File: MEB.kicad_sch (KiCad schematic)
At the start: 6 parts, among them J7 171857-0003, J8 171856-0004

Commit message: Cleanup symbol field table
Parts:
- D2: ALTIUM_VALUE 3.2V -> (none); DATASHEET LINK https://www.we-online.com/katalog/datasheet/150080BS75000.p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 -> (none); MANUFACTURER Würth Elektronik -> (none); MANUFACTURER PART NUMBER 150080BS75000 -> (none); OPERATING TEMPERATURE -40°C ~ 85°C -> (none); PACKAGE / CASE 0805 (2012 Metric) -> (none); Part Number (none) -> 150080BS75000; ROHS YES -> (none)
- D3: ALTIUM_VALUE 3.2V -> (none); DATASHEET LINK https://www.we-online.com/katalog/datasheet/150080GS75000.p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 -> (none); MANUFACTURER Würth Elektronik -> (none); MANUFACTURER PART NUMBER 150080GS75000 -> (none); OPERATING TEMPERATURE -40°C ~ 85°C -> (none); PACKAGE / CASE 0805 (2012 Metric) -> (none); Part Number (none) -> 150080GS75000; ROHS YES -> (none)
- J7: ALTIUM_VALUE 1x3 -> (none); DATASHEET LINK https://componentsearchengine.com//171857-0003.pdf -> (none); MANUFACTURER Molex -> (none); MANUFACTURER PART NUMBER 171857-0003 -> (none); MANUFACTURER_NAME Molex -> (none); MOUSER2 PART NUMBER 538-171857-0003 -> (none); MOUSER2 PRICE/STOCK https://www.mouser.com/Search/Refine.aspx?Keyword=538-17185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 -> (none); Part Number (none) -> 171857-0003
- J8: ALTIUM_VALUE 1x4 -> (none); DATASHEET LINK https://www.molex.com/pdm_docs/sd/1718560004_sd.pdf -> (none); HEIGHT 11.05mm -> (none); MANUFACTURER Molex -> (none); MANUFACTURER PART NUMBER 171856-0004 -> (none); MANUFACTURER_NAME Molex -> (none); Part Number (none) -> 171856-0004
- R11: ALTIUM_VALUE 1.3k -> (none); DATASHEET LINK https://www.koaspeer.com/pdfs/RK73B.pdf -> (none); MANUFACTURER KOA Speer Electronics, Inc. -> (none); MANUFACTURER PART NUMBER RK73B2ATTD132J -> (none); OPERATING TEMPERATURE -55°C ~ 155°C -> (none); PACKAGE / CASE 0805 (2012 Metric) -> (none); Part Number (none) -> RK73B2ATTD132J; ROHS YES -> (none)
- R12: ALTIUM_VALUE 10 -> (none); DATASHEET LINK https://www.yageo.com/upload/media/product/productsearch/da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 -> (none); MANUFACTURER YAGEO -> (none); MANUFACTURER PART NUMBER RC0805FR-0710RL -> (none); OPERATING TEMPERATURE -55°C ~ 155°C -> (none); PACKAGE / CASE 0805 (2012 Metric) -> (none); Part Number (none) -> RC0805FR-0710RL; ROHS YES -> (none)

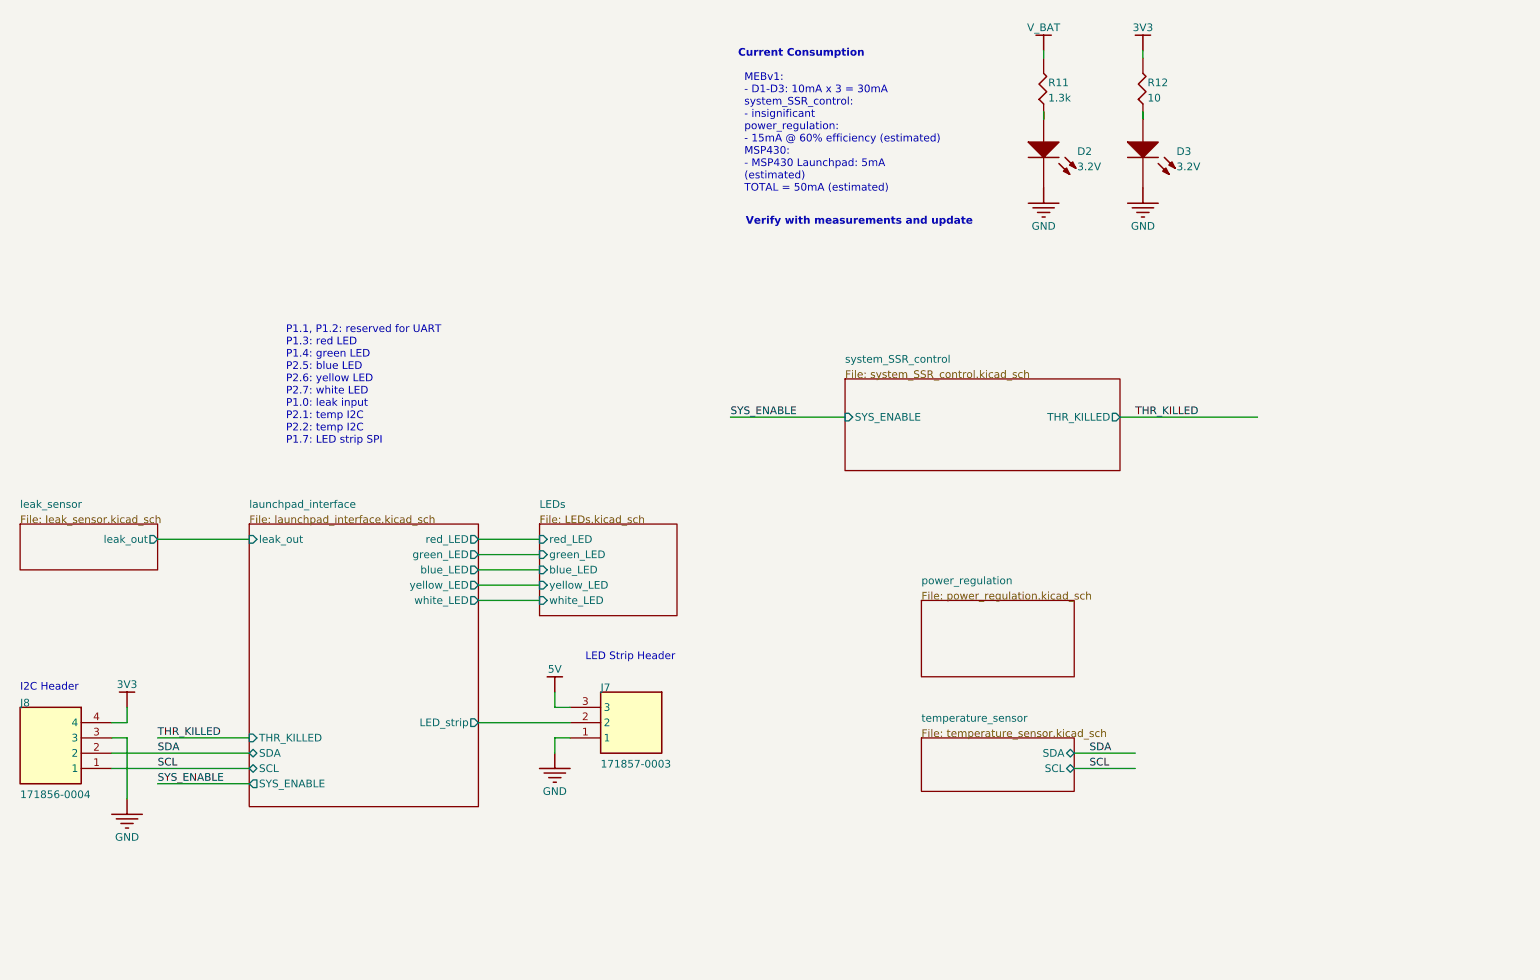
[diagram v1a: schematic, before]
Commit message: Input and Output Header Updates to MEB
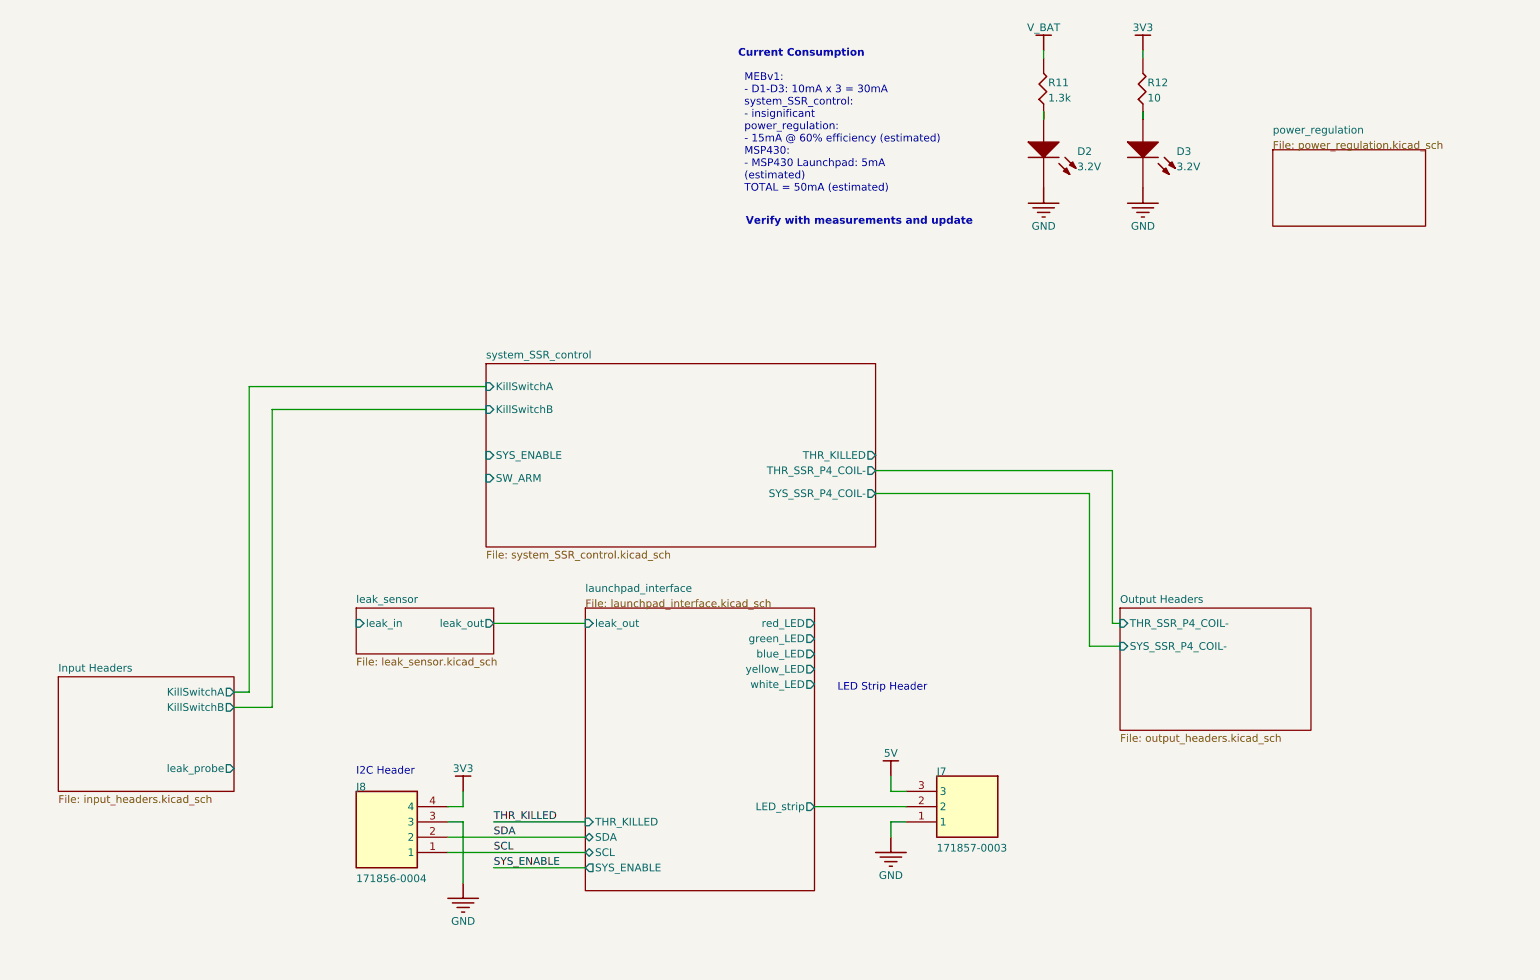
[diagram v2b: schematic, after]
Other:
- removed sheet LEDs
- removed sheet temperature_sensor
- added sheet Input Headers (input_headers.kicad_sch)
- added sheet Output Headers (output_headers.kicad_sch)
- sheet leak_sensor ports: added leak_in; removed none
- sheet system_SSR_control ports: added KillSwitchA, KillSwitchB, SW_ARM, SYS_SSR_P4_COIL-, THR_SSR_P4_COIL-; removed none
- moved on the sheet: J7, J8

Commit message: Finished updating all input and output headers
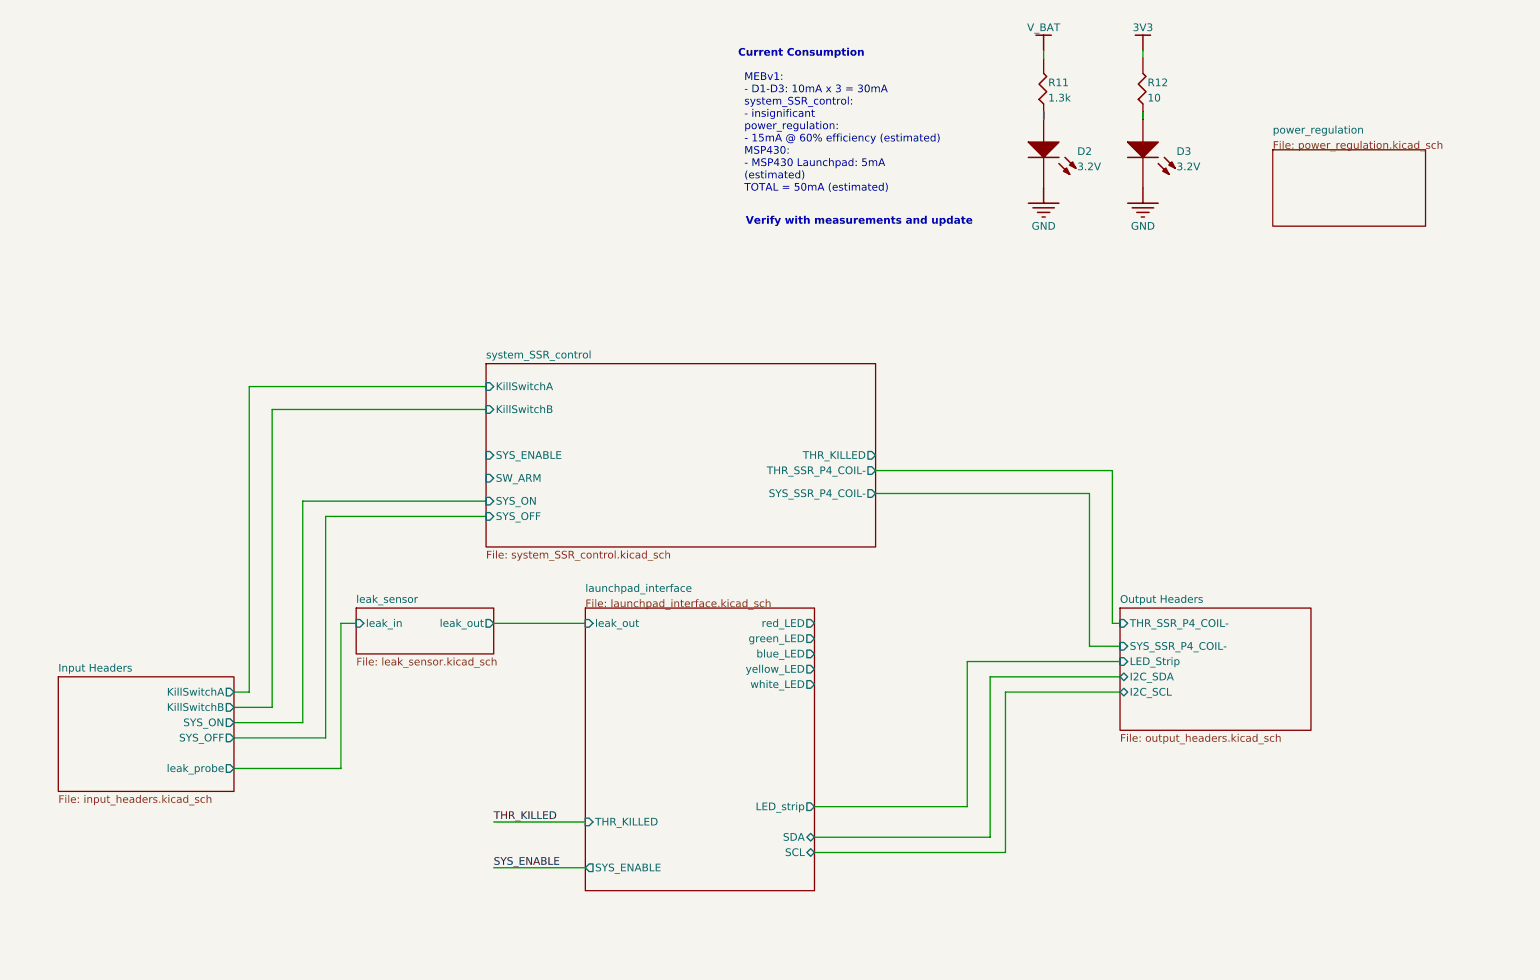
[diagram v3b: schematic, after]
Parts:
- removed J7: 171857-0003, AltiumImport:171857-0003, symbol MEB-altium-import:root_0_171857-0003
- removed J8: 171856-0004, AltiumImport:SHDR4W99P0X254_1X4_1001X635X1105P, symbol MEB-altium-import:root_2_171856-0004
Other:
- sheet Input Headers ports: added SYS_OFF, SYS_ON; removed none
- sheet Output Headers ports: added I2C_SCL, I2C_SDA, LED_Strip; removed none
- sheet system_SSR_control ports: added SYS_OFF, SYS_ON; removed none
- note removed: "I2C Header"
- note removed: "LED Strip Header"

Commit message: Started Working on MCU Interface
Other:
- sheet launchpad_interface renamed mcu_interface
- sheet mcu_interface: file launchpad_interface.kicad_sch -> mcu_interface.kicad_sch
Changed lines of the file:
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@@
     (stroke (width 0) (type solid) (color 128 0 0 1))
     (fill (color 255 153 0 1.0000))
-    (property "Sheetname" "launchpad_interface" (at 114.3 151.13 0)
+    (property "Sheetname" "mcu_interface" (at 114.3 151.13 0)
       (effects (font (size 1.27 1.27)) (justify left bottom))
     )
-    (property "Sheetfile" "launchpad_interface.kicad_sch" (at 114.3 153.67 0)
+    (property "Sheetfile" "mcu_interface.kicad_sch" (at 114.3 153.67 0)
       (effects (font (size 1.27 1.27)) (justify left bottom))
     )

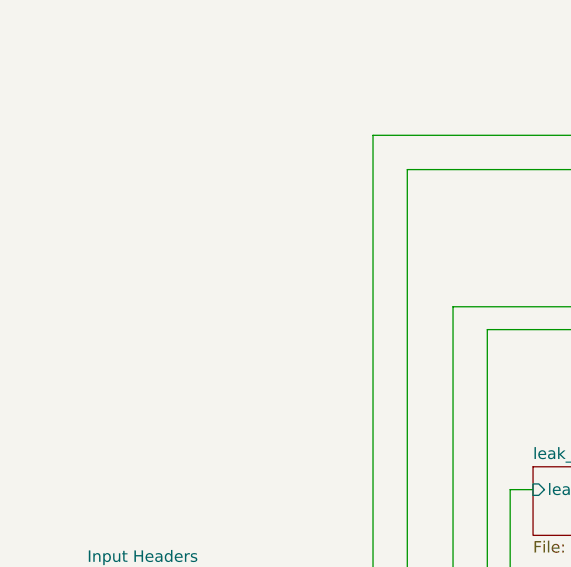
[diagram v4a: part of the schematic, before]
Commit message: Added Temp Sensor
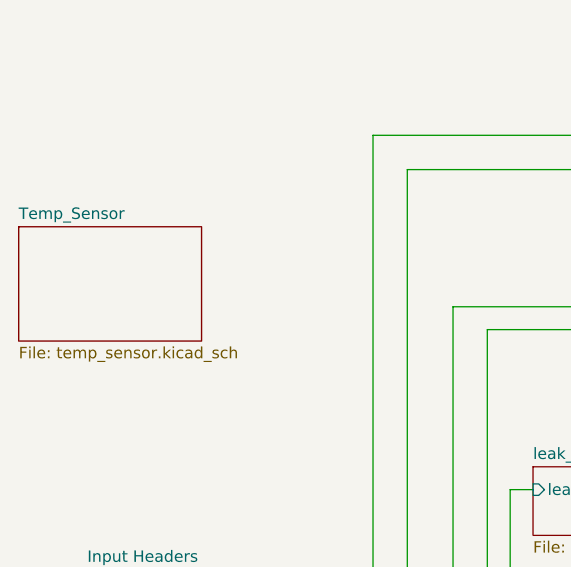
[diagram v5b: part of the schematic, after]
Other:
- added sheet Temp_Sensor (temp_sensor.kicad_sch)
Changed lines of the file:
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@@
+    )
+  )
+  (sheet (at 19.05 127) (size 20.32 12.7) (fields_autoplaced)
+    (stroke (width 0.1524) (type solid))
+    (fill (color 0 0 0 0.0000))
+    (property "Sheetname" "Temp_Sensor" (at 19.05 126.2884 0)
+      (effects (font (size 1.27 1.27)) (justify left bottom))
+    )
+    (property "Sheetfile" "temp_sensor.kicad_sch" (at 19.05 140.2846 0)
+      (effects (font (size 1.27 1.27)) (justify left top))
+    )
+    (instances
+      (project "MEB"
+        (path "/228e4997-23c1-4c21-939b-583cad26a5e3" (page "8"))
+      )
     )
   )

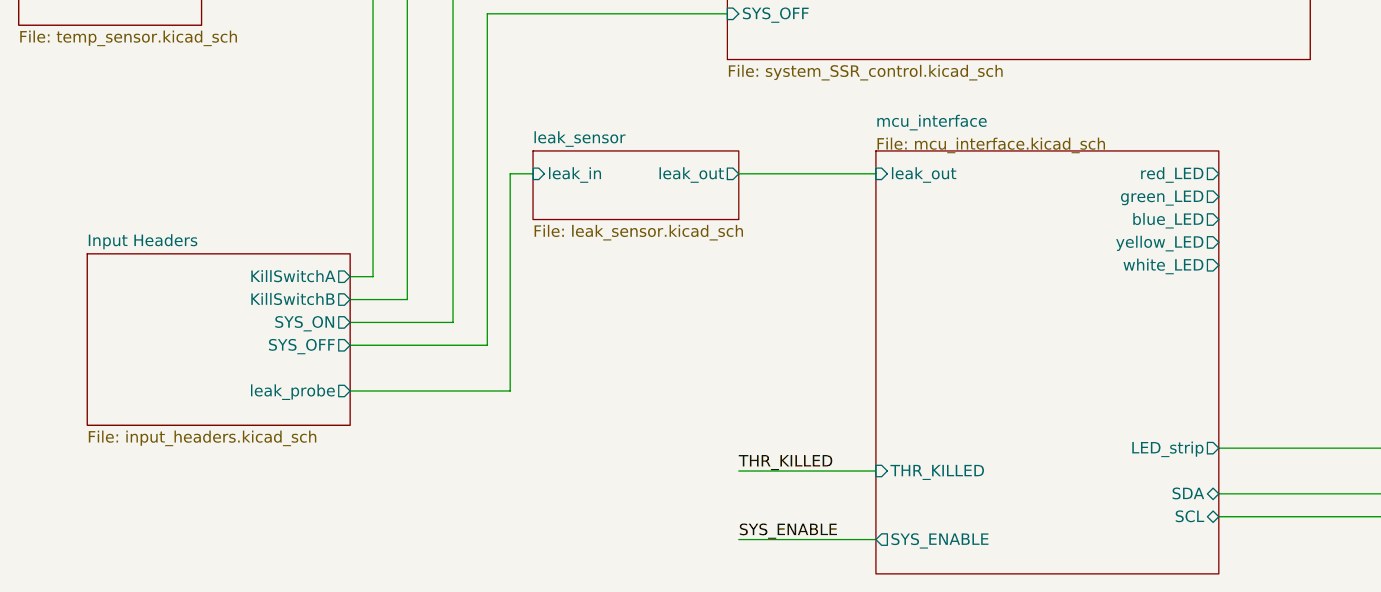
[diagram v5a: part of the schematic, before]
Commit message: updated input headers schematic for FT232 chip
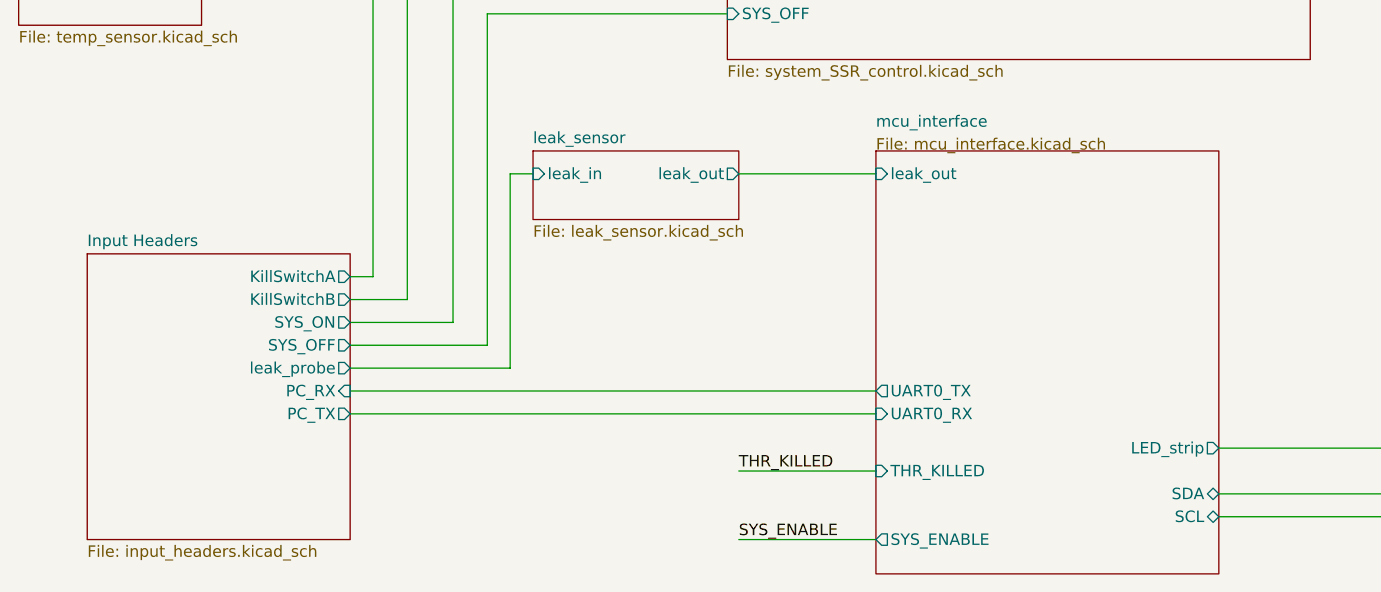
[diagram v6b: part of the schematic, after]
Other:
- sheet Input Headers ports: added PC_RX, PC_TX; removed none
- sheet mcu_interface ports: added UART0_RX, UART0_TX; removed blue_LED, green_LED, red_LED, white_LED, yellow_LED
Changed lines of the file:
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@@
+    (stroke (width 0) (type default))
+  )
+  (wire (pts (xy 55.88 180.34) (xy 114.3 180.34))
     (stroke (width 0) (type default))
   )
@@
     (stroke (width 0) (type default))
   )
-  (wire (pts (xy 55.88 180.34) (xy 73.66 180.34))
+  (wire (pts (xy 55.88 177.8) (xy 73.66 177.8))
     (stroke (width 0) (type default))
   )
@@
     (stroke (width 0) (type default))
   )
-  (wire (pts (xy 73.66 180.34) (xy 73.66 156.21))
+  (wire (pts (xy 73.66 177.8) (xy 73.66 156.21))
     (stroke (width 0) (type default))
   )
@@
   (wire (pts (xy 207.01 60.96) (xy 207.01 62.23))
     (stroke (width 0.254) (type default))
+  )
+  (wire (pts (xy 55.88 182.88) (xy 114.3 182.88))
+    (stroke (width 0) (type default))
   )
   (wire (pts (xy 198.12 134.62) (xy 198.12 160.02))
@@
       (effects (font (size 1.27 1.27)) (justify right))
     )
-    (pin "red_LED" output (at 152.4 156.21 0)
-      (effects (font (size 1.27 1.27)) (justify right))
-    )
-    (pin "green_LED" output (at 152.4 158.75 0)
-      (effects (font (size 1.27 1.27)) (justify right))
-    )
-    (pin "blue_LED" output (at 152.4 161.29 0)
-      (effects (font (size 1.27 1.27)) (justify right))
-    )
-    (pin "yellow_LED" output (at 152.4 163.83 0)
-      (effects (font (size 1.27 1.27)) (justify right))
-    )
-    (pin "white_LED" output (at 152.4 166.37 0)
-      (effects (font (size 1.27 1.27)) (justify right))
-    )
     (pin "SCL" bidirectional (at 152.4 194.31 0)
       (effects (font (size 1.27 1.27)) (justify right))
@@
     )
     (pin "THR_KILLED" input (at 114.3 189.23 180)
+      (effects (font (size 1.27 1.27)) (justify left))
+    )
+    (pin "UART0_TX" output (at 114.3 180.34 180)
+      (effects (font (size 1.27 1.27)) (justify left))
+    )
+    (pin "UART0_RX" input (at 114.3 182.88 180)
       (effects (font (size 1.27 1.27)) (justify left))
     )
@@
     )
   )
-  (sheet (at 26.67 165.1) (size 29.21 19.05) (fields_autoplaced)
+  (sheet (at 26.67 165.1) (size 29.21 31.75) (fields_autoplaced)
     (stroke (width 0.1524) (type solid))
     (fill (color 0 0 0 0.0000))
@@
       (effects (font (size 1.27 1.27)) (justify left bottom))
     )
-    (property "Sheetfile" "input_headers.kicad_sch" (at 26.67 184.7346 0) (show_name)
+    (property "Sheetfile" "input_headers.kicad_sch" (at 26.67 197.4346 0) (show_name)
       (effects (font (size 1.27 1.27)) (justify left top))
     )
-    (pin "leak_probe" output (at 55.88 180.34 0)
+    (pin "leak_probe" output (at 55.88 177.8 0)
       (effects (font (size 1.27 1.27)) (justify right))
     )
@@
       (effects (font (size 1.27 1.27)) (justify right))
     )
+    (pin "PC_TX" output (at 55.88 182.88 0)
+      (effects (font (size 1.27 1.27)) (justify right))
+    )
+    (pin "PC_RX" input (at 55.88 180.34 0)
+      (effects (font (size 1.27 1.27)) (justify right))
+    )
